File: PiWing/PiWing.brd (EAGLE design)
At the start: 100 x 80 mm, 6 parts, among them J1 RASPBERRYPI-40-PIN-GPIO_PTH

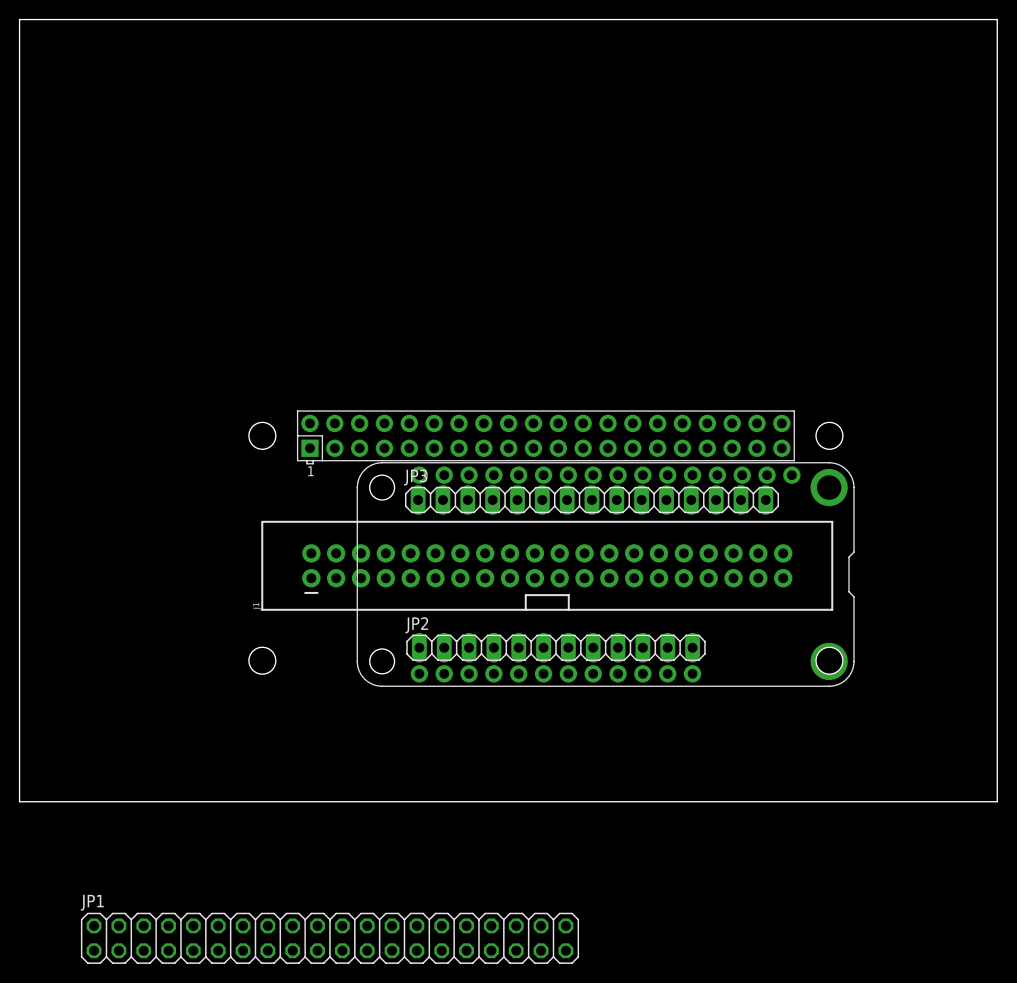
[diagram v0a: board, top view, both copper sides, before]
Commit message: Adding Pi Wing
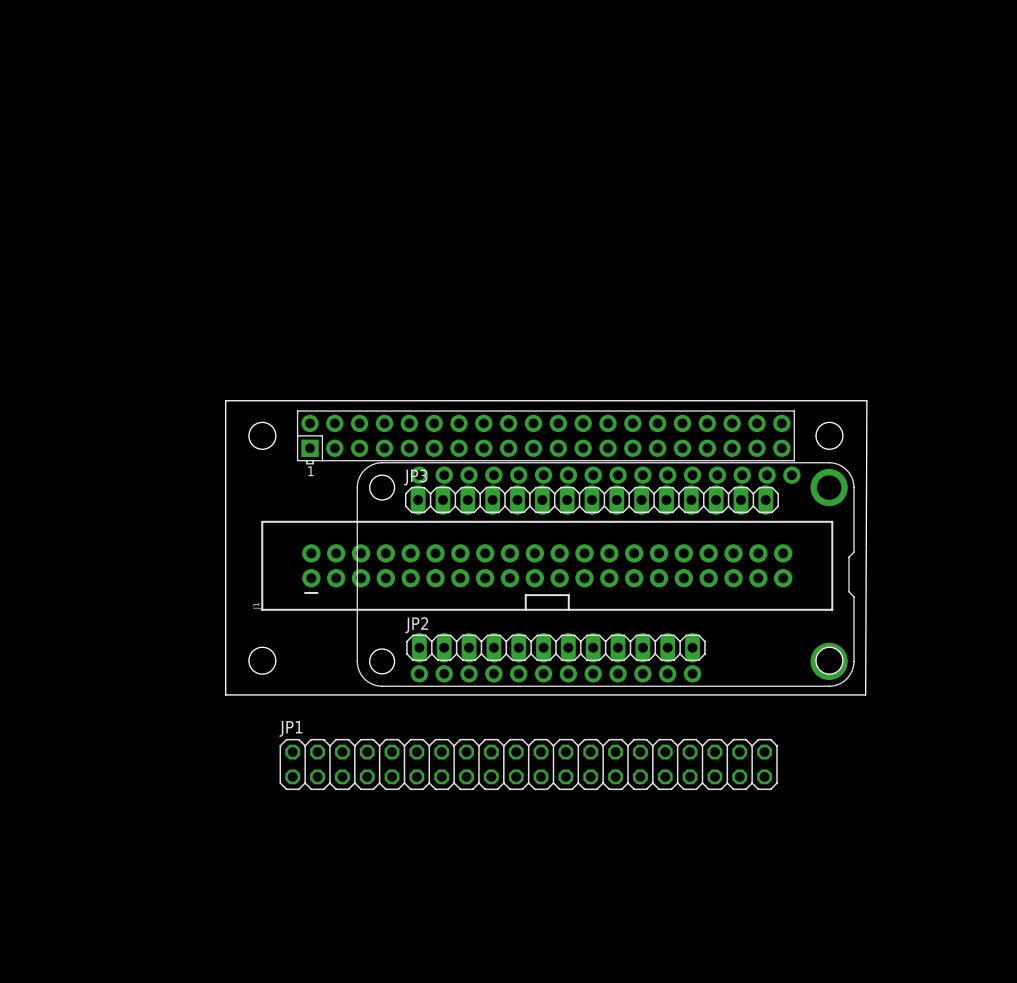
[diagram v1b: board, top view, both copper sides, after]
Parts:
- moved JP1 27.0 mm to (52.1, 3.81)
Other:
- board size 100 x 80 mm -> 65.6 x 30.1 mm
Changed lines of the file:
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@@
 <layer number="43" name="vRestrict" color="2" fill="10" visible="yes" active="yes"/>
 <layer number="44" name="Drills" color="7" fill="1" visible="no" active="yes"/>
-<layer number="45" name="Holes" color="7" fill="1" visible="no" active="yes"/>
+<layer number="45" name="Holes" color="7" fill="1" visible="yes" active="yes"/>
 <layer number="46" name="Milling" color="3" fill="1" visible="no" active="yes"/>
 <layer number="47" name="Measures" color="7" fill="1" visible="no" active="yes"/>
@@
 <board>
 <plain>
-<wire x1="0" y1="0" x2="100" y2="0" width="0" layer="20"/>
-<wire x1="100" y1="0" x2="100" y2="80" width="0" layer="20"/>
-<wire x1="100" y1="80" x2="0" y2="80" width="0" layer="20"/>
-<wire x1="0" y1="80" x2="0" y2="0" width="0" layer="20"/>
+<wire x1="21.082" y1="10.922" x2="86.538" y2="10.922" width="0" layer="20"/>
+<wire x1="86.538" y1="10.922" x2="86.665" y2="41.011" width="0" layer="20"/>
+<wire x1="86.665" y1="41.011" x2="21.082" y2="41.011" width="0" layer="20"/>
+<wire x1="21.082" y1="41.011" x2="21.082" y2="10.922" width="0" layer="20"/>
 </plain>
 <attributes>
@@
 <attribute name="SF_ID" value="PRT-13054" x="53.975" y="24.13" size="1.778" layer="27" rot="R90" display="off"/>
 </element>
-<element name="JP1" library="adafruit" library_urn="urn:adsk.eagle:library:420" package="2X20" value="" x="31.75" y="-13.97"/>
+<element name="JP1" library="adafruit" library_urn="urn:adsk.eagle:library:420" package="2X20" value="" x="52.07" y="3.81"/>
 <element name="JP2" library="adafruit" library_urn="urn:adsk.eagle:library:420" package="1X12" value="" x="54.864" y="15.748"/>
 <element name="JP3" library="adafruit" library_urn="urn:adsk.eagle:library:420" package="1X15" value="" x="58.547" y="30.861"/>
